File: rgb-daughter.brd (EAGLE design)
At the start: 226.1 x 74 mm, 103 parts

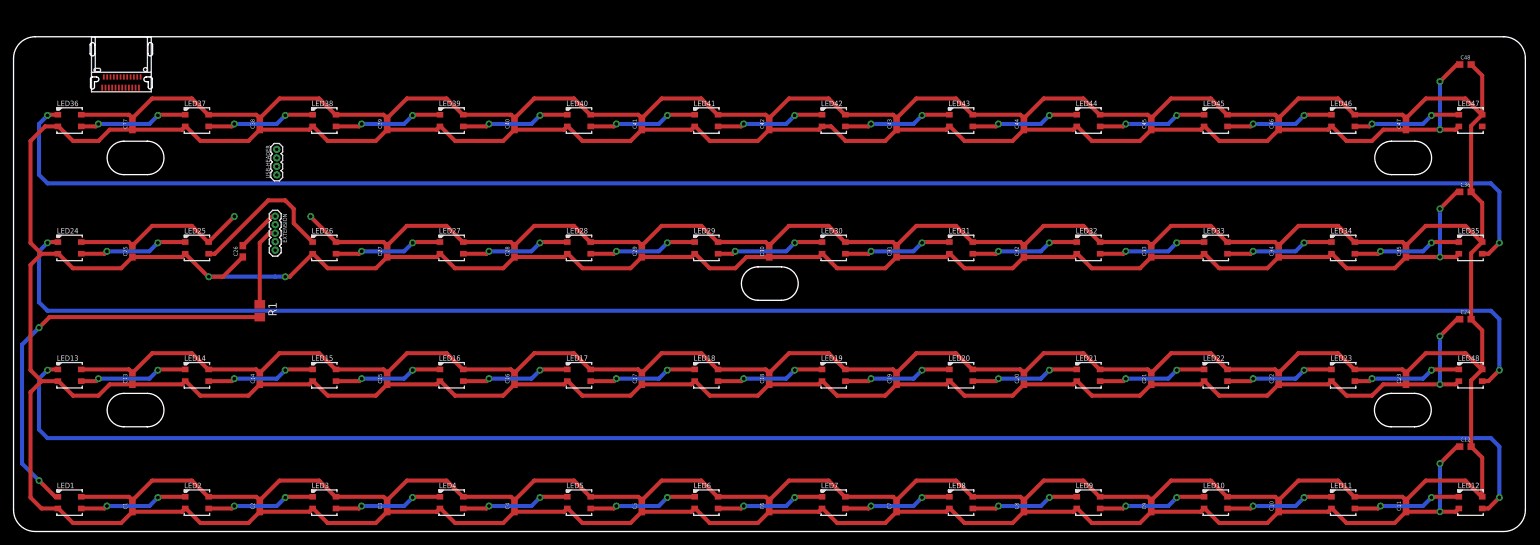
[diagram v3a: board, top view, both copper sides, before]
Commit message: 👽 update for new USB-C package
- connect new pins on USB-C
- move USB-C package to match placement in case
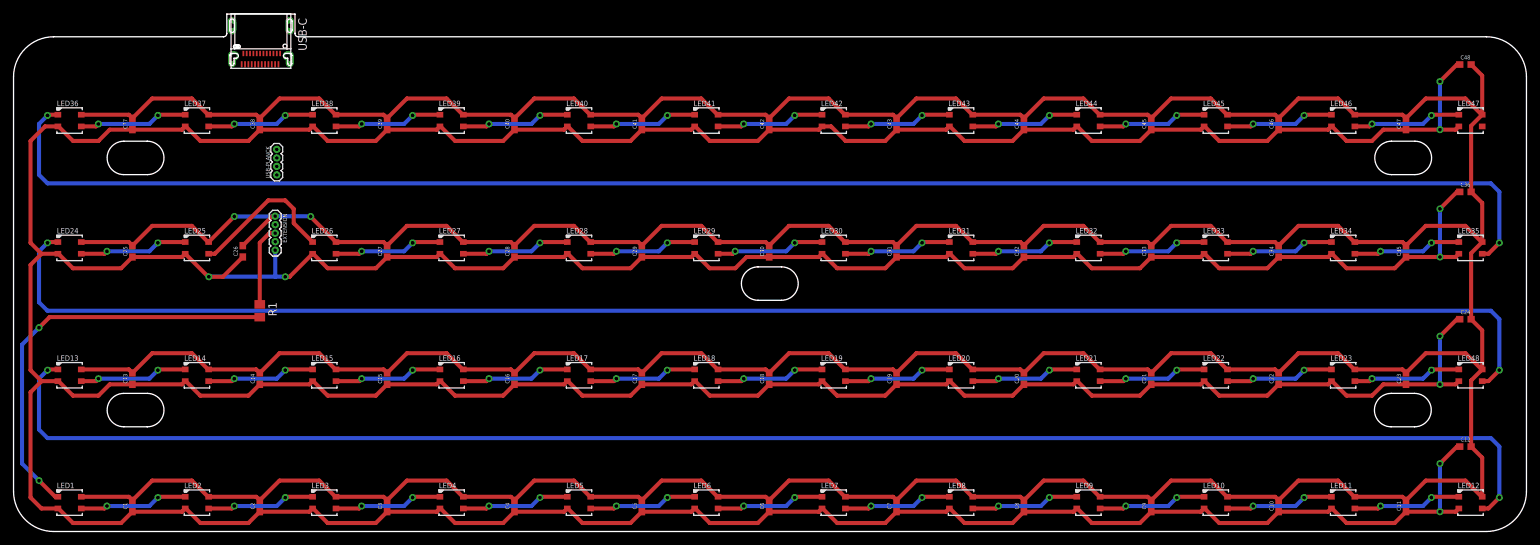
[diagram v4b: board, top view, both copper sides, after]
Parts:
- removed U$1: USB-TYPE-CDX07S024JJ3R1300, usb:DX07S024JJ3R1300
- added USB-C: USB-TYPE-CDX07S024JJ3R1300, usb:DX07S024JJ3R1300
- moved FRAME3 148.0 mm to (158.2, -27.9)
- moved FRAME1 4.00 mm to (178.7, 45.3)
- renumbered USB-HEADER to USB-PLANCK
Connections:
- removed net USB-D+: U$1.A6, U$1.B6, USB-PLANCK.2
- removed net USB-D-: U$1.A7, U$1.B7, USB-PLANCK.3
- new net USB_D+: USB-C.A7, USB-C.B7, USB-PLANCK.2
- new net USB_D-: USB-C.A6, USB-C.B6, USB-PLANCK.3
- net GND: now also USB-C.A1, USB-C.A12, USB-C.B1, USB-C.B12, USB-C.GND$1, USB-C.GND$2, USB-C.GND$3, USB-C.GND$4, USB-C.GND$5, USB-C.GND$6; no longer U$1.A1, U$1.A12, U$1.B1, U$1.B12
- net VDD: now also USB-C.A4, USB-C.A9, USB-C.B4, USB-C.B9; no longer U$1.A4, U$1.A9, U$1.B4, U$1.B9
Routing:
- net GND: track 1011.2 -> 1022.6 mm
- net VDD: track 1040.4 -> 1044.3 mm
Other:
- board size 226.1 x 74 mm -> 226.3 x 77.4 mm

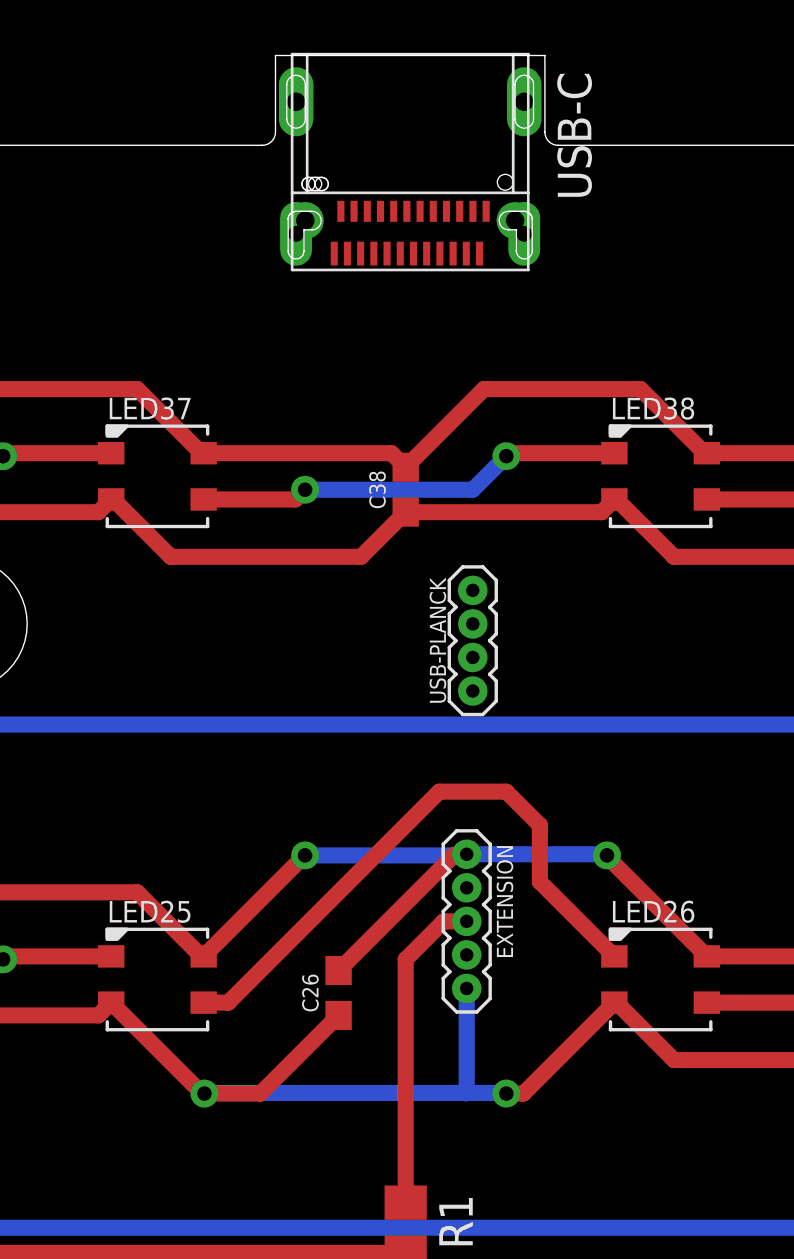
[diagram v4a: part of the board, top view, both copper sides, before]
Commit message: 🚧✨ routing USB-C connector
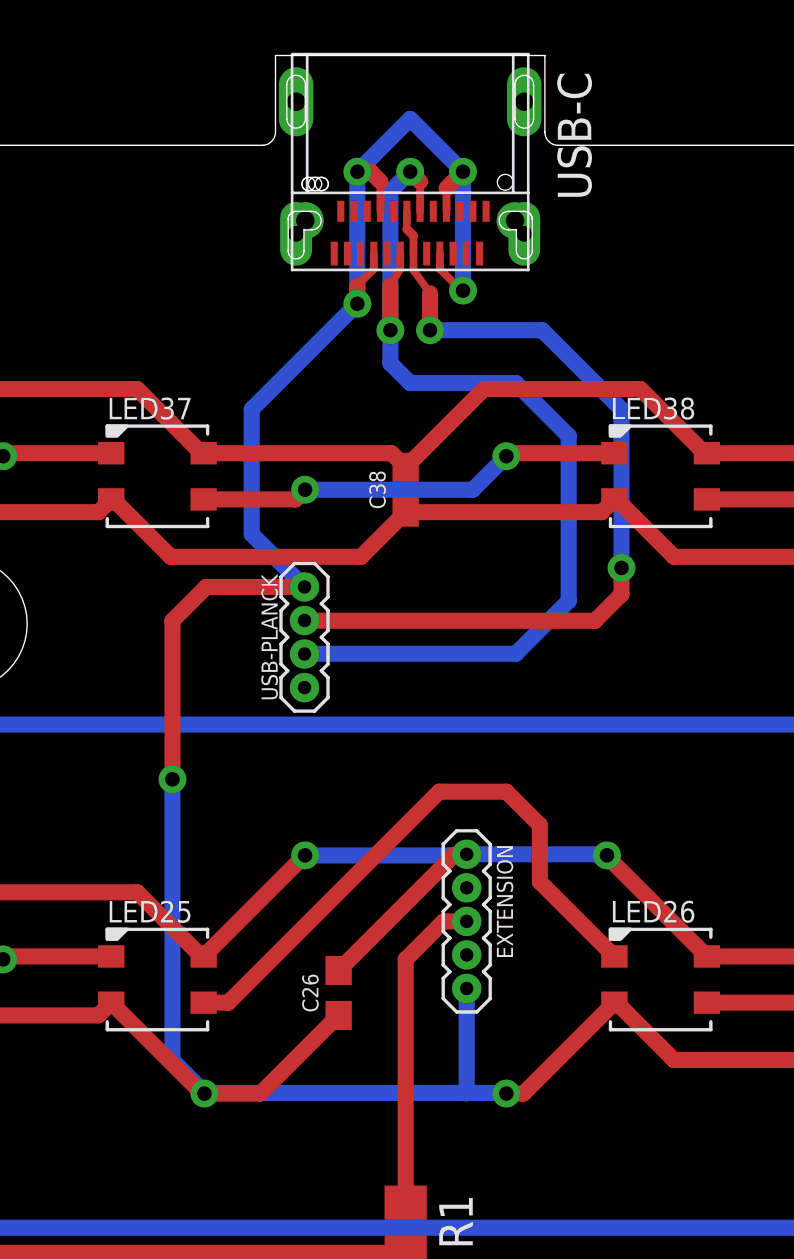
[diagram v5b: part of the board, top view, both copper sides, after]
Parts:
- moved USB-PLANCK 6.37 mm to (33.0, 53.5)
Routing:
- net VDD: track 1044.3 -> 1104.5 mm, vias 10 -> 15
- net USB_D+: track 0.00 -> 37.2 mm, vias 0 -> 2
- net USB_D-: track 0.00 -> 32.7 mm, vias 0 -> 2
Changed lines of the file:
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@@
 <setting verticaltext="up"/>
 </settings>
-<grid distance="1" unitdist="mm" unit="mm" style="lines" multiple="1" display="yes" altdistance="0.1" altunitdist="mm" altunit="mm"/>
+<grid distance="1" unitdist="mm" unit="mm" style="lines" multiple="1" display="yes" altdistance="0.25" altunitdist="mm" altunit="mm"/>
 <layers>
 <layer number="1" name="Top" color="4" fill="1" visible="yes" active="yes"/>
@@
 <element name="FRAME3" library="SparkFun-Aesthetics" library_urn="urn:adsk.eagle:library:507" package="CREATIVE_COMMONS" package3d_urn="urn:adsk.eagle:package:37121/1" value="FRAME-LETTER" x="158.16" y="-27.94"/>
 <element name="USB-C" library="usb" package="DX07S024JJ3R1300" value="USB-TYPE-CDX07S024JJ3R1300" x="37" y="72.6" rot="R180"/>
-<element name="USB-PLANCK" library="SparkFun-Connectors" library_urn="urn:adsk.eagle:library:513" package="1X04_1.27MM" package3d_urn="urn:adsk.eagle:package:38086/1" value="" x="39.37" y="53.34" rot="R90"/>
+<element name="USB-PLANCK" library="SparkFun-Connectors" library_urn="urn:adsk.eagle:library:513" package="1X04_1.27MM" package3d_urn="urn:adsk.eagle:package:38086/1" value="" x="33" y="53.47" rot="R90"/>
 </elements>
 <signals>
@@
 <wire x1="39.096984375" y1="47.117" x2="39.1395625" y2="47.159578125" width="0.6096" layer="16"/>
 <wire x1="39.1395625" y1="47.159578125" x2="44.407421875" y2="47.159578125" width="0.6096" layer="16"/>
-<wire x1="39.1395625" y1="47.159578125" x2="39.37" y2="53.34" width="0" layer="19" extent="1-1"/>
+<wire x1="39.875" y1="71.5" x2="41.318" y2="75.648" width="0" layer="19" extent="1-1"/>
+<wire x1="40.97" y1="71.15" x2="39.875" y2="71.5" width="0" layer="19" extent="1-1"/>
+<wire x1="41.318" y1="70.648" x2="40.97" y2="71.15" width="0" layer="19" extent="1-1"/>
+<wire x1="39.625" y1="69.9" x2="39.875" y2="71.5" width="0" layer="19" extent="1-1"/>
+<wire x1="39.79" y1="64.77" x2="39.625" y2="69.9" width="0" layer="19" extent="1-1"/>
 <wire x1="38.689578125" y1="47.159578125" x2="39.096984375" y2="47.117" width="0" layer="19" extent="1-16"/>
-<wire x1="41.318" y1="70.648" x2="20.74" y2="64.77" width="0" layer="19" extent="1-1"/>
-<wire x1="40.97" y1="71.15" x2="41.318" y2="70.648" width="0" layer="19" extent="1-1"/>
-<wire x1="39.875" y1="71.5" x2="40.97" y2="71.15" width="0" layer="19" extent="1-1"/>
-<wire x1="39.625" y1="69.9" x2="39.875" y2="71.5" width="0" layer="19" extent="1-1"/>
-<wire x1="41.318" y1="75.648" x2="39.875" y2="71.5" width="0" layer="19" extent="1-1"/>
-<wire x1="32.682" y1="70.648" x2="10.132" y2="62.343" width="0" layer="19" extent="1-1"/>
-<wire x1="33.03" y1="71.15" x2="32.682" y2="70.648" width="0" layer="19" extent="1-1"/>
-<wire x1="34.375" y1="71.5" x2="33.03" y2="71.15" width="0" layer="19" extent="1-1"/>
-<wire x1="34.125" y1="69.9" x2="32.682" y2="70.648" width="0" layer="19" extent="1-1"/>
+<wire x1="34.375" y1="71.5" x2="39.875" y2="71.5" width="0" layer="19" extent="1-1"/>
+<wire x1="33.03" y1="71.15" x2="34.375" y2="71.5" width="0" layer="19" extent="1-1"/>
+<wire x1="32.682" y1="70.648" x2="33.03" y2="71.15" width="0" layer="19" extent="1-1"/>
+<wire x1="34.125" y1="69.9" x2="34.375" y2="71.5" width="0" layer="19" extent="1-1"/>
 <wire x1="32.682" y1="75.648" x2="34.375" y2="71.5" width="0" layer="19" extent="1-1"/>
+<wire x1="33" y1="53.47" x2="33.062578125" y2="47.159578125" width="0" layer="19" extent="16-16"/>
 </signal>
 <signal name="VDD">
@@
 <wire x1="40.64" y1="38.1" x2="41.289" y2="38.1" width="0.6096" layer="1"/>
 <wire x1="41.289" y1="38.1" x2="44.732" y2="41.543" width="0.6096" layer="1"/>
-<wire x1="39.1395625" y1="38.1235625" x2="29.2335625" y2="38.1235625" width="0.6096" layer="16"/>
+<wire x1="29.2335625" y1="38.1235625" x2="39.1395625" y2="38.1235625" width="0.6096" layer="16"/>
 <wire x1="29.2335625" y1="38.1235625" x2="29.21" y2="38.1" width="0.6096" layer="16"/>
 <via x="29.21" y="38.1" extent="1-16" drill="0.55"/>
@@
 <contactref element="USB-C" pad="B4"/>
 <wire x1="39.1395625" y1="42.079578125" x2="39.1395625" y2="38.1235625" width="0.6096" layer="16"/>
-<wire x1="36.83" y1="60.11" x2="39.37" y2="57.15" width="0" layer="19" extent="1-1"/>
-<wire x1="35.625" y1="69.9" x2="14.39" y2="60.11" width="0" layer="19" extent="1-1"/>
-<wire x1="35.875" y1="71.5" x2="35.625" y2="69.9" width="0" layer="19" extent="1-1"/>
-<wire x1="38.125" y1="69.9" x2="35.625" y2="69.9" width="0" layer="19" extent="1-1"/>
-<wire x1="38.375" y1="71.5" x2="38.125" y2="69.9" width="0" layer="19" extent="1-1"/>
+<wire x1="35" y1="68.6905" x2="35" y2="68" width="0.6096" layer="1"/>
+<wire x1="35.625" y1="69.9" x2="35.625" y2="69.3155" width="0.3" layer="1"/>
+<wire x1="35.625" y1="69.3155" x2="35" y2="68.6905" width="0.3" layer="1"/>
+<wire x1="38.125" y1="69.9" x2="38.125" y2="69.3155" width="0.3" layer="1"/>
+<via x="35" y="68" extent="1-16" drill="0.55"/>
+<via x="39" y="68.5" extent="1-16" drill="0.55"/>
+<wire x1="38.375" y1="71.5" x2="38.375" y2="72.375" width="0.3" layer="1"/>
+<wire x1="38.375" y1="72.375" x2="39" y2="73" width="0.6096" layer="1"/>
+<via x="39" y="73" extent="1-16" drill="0.55"/>
+<wire x1="39" y1="68.5" x2="39" y2="73" width="0.6096" layer="16"/>
+<via x="35" y="73" extent="1-16" drill="0.55"/>
+<wire x1="35" y1="73" x2="35" y2="68" width="0.6096" layer="16"/>
+<wire x1="35.875" y1="71.5" x2="35.875" y2="72.625" width="0.3" layer="1"/>
+<wire x1="35.875" y1="72.625" x2="35.5" y2="73" width="0.6096" layer="1"/>
+<wire x1="35.5" y1="73" x2="35" y2="73" width="0.6096" layer="1"/>
+<wire x1="35" y1="68" x2="31" y2="64" width="0.6096" layer="16"/>
+<wire x1="31" y1="64" x2="31" y2="59.28" width="0.6096" layer="16"/>
+<wire x1="31" y1="59.28" x2="33" y2="57.28" width="0.6096" layer="16"/>
+<wire x1="39" y1="73" x2="37" y2="75" width="0.6096" layer="16"/>
+<wire x1="37" y1="75" x2="35" y2="73" width="0.6096" layer="16"/>
+<wire x1="38.125" y1="69.3155" x2="38.9405" y2="68.5" width="0.3" layer="1"/>
+<wire x1="38.9405" y1="68.5" x2="39" y2="68.5" width="0.3" layer="1"/>
+<wire x1="33" y1="57.28" x2="29.28" y2="57.28" width="0.6096" layer="1"/>
+<wire x1="29.28" y1="57.28" x2="28" y2="56" width="0.6096" layer="1"/>
+<wire x1="28" y1="56" x2="28" y2="50" width="0.6096" layer="1"/>
+<via x="28" y="50" extent="1-16" drill="0.55"/>
+<wire x1="28" y1="50" x2="28" y2="39.357125" width="0.6096" layer="16"/>
+<wire x1="28" y1="39.357125" x2="29.2335625" y2="38.1235625" width="0.6096" layer="16"/>
 </signal>
 <signal name="N$3">
@@
 <contactref element="USB-C" pad="B6"/>
 <contactref element="USB-PLANCK" pad="3"/>
-<wire x1="37.125" y1="69.9" x2="39.37" y2="55.88" width="0" layer="19" extent="1-1"/>
-<wire x1="36.875" y1="71.5" x2="37.125" y2="69.9" width="0" layer="19" extent="1-1"/>
+<wire x1="37.125" y1="70.575" x2="37.125" y2="69.9" width="0.3" layer="1"/>
+<wire x1="36.875" y1="71.5" x2="36.875" y2="70.825" width="0.29" layer="1"/>
+<wire x1="36.875" y1="70.825" x2="37.125" y2="70.575" width="0.35" layer="1"/>
+<wire x1="37.125" y1="69.275" x2="37.75" y2="68.4" width="0.29" layer="1"/>
+<wire x1="37.75" y1="68.4" x2="37.75" y2="67" width="0.6096" layer="1"/>
+<wire x1="37.125" y1="69.9" x2="37.125" y2="69.275" width="0.29" layer="1"/>
+<via x="37.75" y="67" extent="1-16" drill="0.55"/>
+<wire x1="37.75" y1="67" x2="42" y2="67" width="0.6096" layer="16"/>
+<wire x1="42" y1="67" x2="45" y2="64" width="0.6096" layer="16"/>
+<wire x1="45" y1="64" x2="45" y2="58" width="0.6096" layer="16"/>
+<via x="45" y="58" extent="1-16" drill="0.55"/>
+<wire x1="45" y1="58" x2="45" y2="57" width="0.6096" layer="1"/>
+<wire x1="45" y1="57" x2="44" y2="56" width="0.6096" layer="1"/>
+<wire x1="44" y1="56" x2="33.01" y2="56" width="0.6096" layer="1"/>
+<wire x1="33.01" y1="56" x2="33" y2="56.01" width="0.6096" layer="1"/>
 </signal>
 <signal name="USB_D+">
@@
 <contactref element="USB-C" pad="B7"/>
 <contactref element="USB-PLANCK" pad="2"/>
-<wire x1="36.625" y1="69.9" x2="39.37" y2="54.61" width="0" layer="19" extent="1-1"/>
-<wire x1="37.375" y1="71.5" x2="36.625" y2="69.9" width="0" layer="19" extent="1-1"/>
+<wire x1="36.25" y1="68.6905" x2="36.25" y2="67" width="0.6096" layer="1"/>
+<wire x1="36.625" y1="69.9" x2="36.625" y2="69.3155" width="0.29" layer="1"/>
+<wire x1="36.625" y1="69.3155" x2="36.25" y2="68.6905" width="0.29" layer="1"/>
+<via x="36.25" y="67" extent="1-16" drill="0.55"/>
+<wire x1="37.375" y1="71.5" x2="37.375" y2="72.625" width="0.29" layer="1"/>
+<wire x1="37.375" y1="72.625" x2="37" y2="73" width="0.6096" layer="1"/>
+<via x="37" y="73" extent="1-16" drill="0.55"/>
+<wire x1="37" y1="73" x2="36.25" y2="72.25" width="0.6096" layer="16"/>
+<wire x1="36.25" y1="72.25" x2="36.25" y2="67" width="0.6096" layer="16"/>
+<wire x1="36.25" y1="67" x2="36.25" y2="65.75" width="0.6096" layer="16"/>
+<wire x1="36.25" y1="65.75" x2="37" y2="65" width="0.6096" layer="16"/>
+<wire x1="37" y1="65" x2="41" y2="65" width="0.6096" layer="16"/>
+<wire x1="41" y1="65" x2="43" y2="63" width="0.6096" layer="16"/>
+<wire x1="43" y1="63" x2="43" y2="56.75" width="0.6096" layer="16"/>
+<wire x1="43" y1="56.75" x2="41" y2="54.75" width="0.6096" layer="16"/>
+<wire x1="41" y1="54.75" x2="33.01" y2="54.75" width="0.6096" layer="16"/>
+<wire x1="33.01" y1="54.75" x2="33" y2="54.74" width="0.6096" layer="16"/>
 </signal>
 </signals>
